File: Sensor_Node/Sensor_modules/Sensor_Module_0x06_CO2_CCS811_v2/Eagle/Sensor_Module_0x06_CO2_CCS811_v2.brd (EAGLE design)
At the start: 55 x 35 mm, 30 parts, among them J1 M04_SMD_90, J2 5.5x2.1mm Barrel, J4 ARDUINO_ISP, U1 CCS811, U2 ATMEGA328P_TQFP, Y1 8MHZ

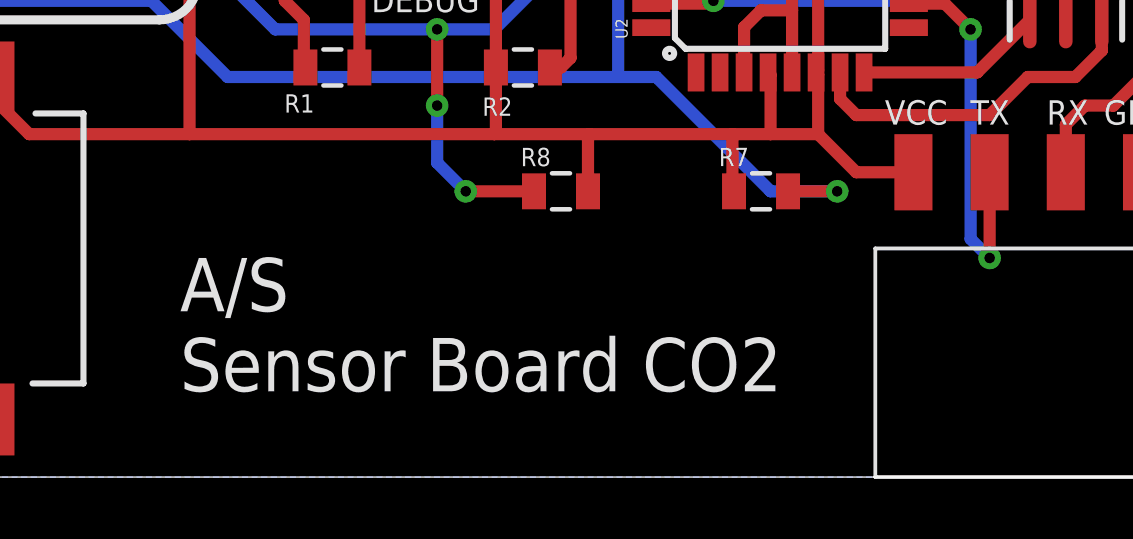
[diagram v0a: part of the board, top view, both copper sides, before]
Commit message: Renaming boards to modules inside eagle files
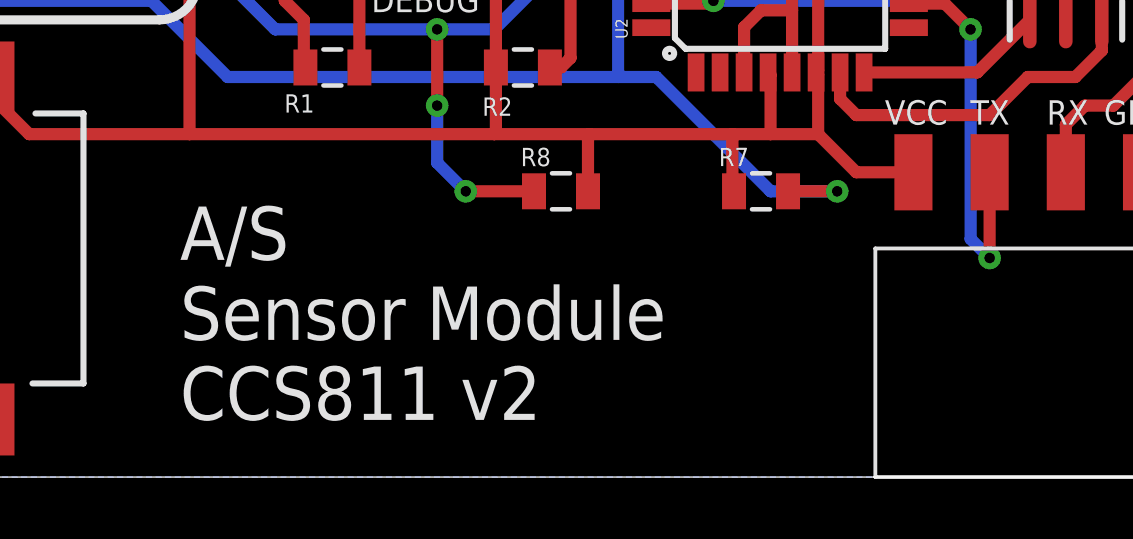
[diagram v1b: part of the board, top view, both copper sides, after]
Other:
- board text added: "A/S Sensor Module CCS811 v2"
- board text removed: "A/S Sensor Board CO2"
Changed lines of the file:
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@@
 <?xml version="1.0" encoding="utf-8"?>
 <!DOCTYPE eagle SYSTEM "eagle.dtd">
-<eagle version="8.5.2">
+<eagle version="9.1.1">
 <drawing>
 <settings>
@@
 <text x="47.625" y="11.7475" size="0.8128" layer="21">RX</text>
 <text x="49.53" y="11.7475" size="0.8128" layer="21">GND</text>
-<text x="18.7325" y="2.8575" size="1.778" layer="21">A/S
-Sensor Board CO2</text>
+<text x="18.7325" y="1.905" size="1.778" layer="21">A/S
+Sensor Module
+CCS811 v2</text>
 <circle x="52.07" y="31.115" radius="1.309084375" width="0.4064" layer="21"/>
 <text x="53.853340625" y="26.9864" size="0.8128" layer="21" rot="R270">VCC</text>
@@
 <param name="checkStop" value="0"/>
 <param name="checkValues" value="0"/>
+<param name="checkNames" value="1"/>
+<param name="checkWireStubs" value="1"/>
+<param name="checkPolygonWidth" value="0"/>
 <param name="useDiameter" value="13"/>
 <param name="maxErrors" value="50"/>
@@
 </signal>
 </signals>
+<mfgpreviewcolors>
+<mfgpreviewcolor name="soldermaskcolor" color="0xC8008000"/>
+<mfgpreviewcolor name="silkscreencolor" color="0xFFFEFEFE"/>
+<mfgpreviewcolor name="backgroundcolor" color="0xFF282828"/>
+<mfgpreviewcolor name="coppercolor" color="0xFFFFBF00"/>
+<mfgpreviewcolor name="substratecolor" color="0xFF786E46"/>
+</mfgpreviewcolors>
 </board>
 </drawing>
